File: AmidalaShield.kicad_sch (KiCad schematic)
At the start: 1 part

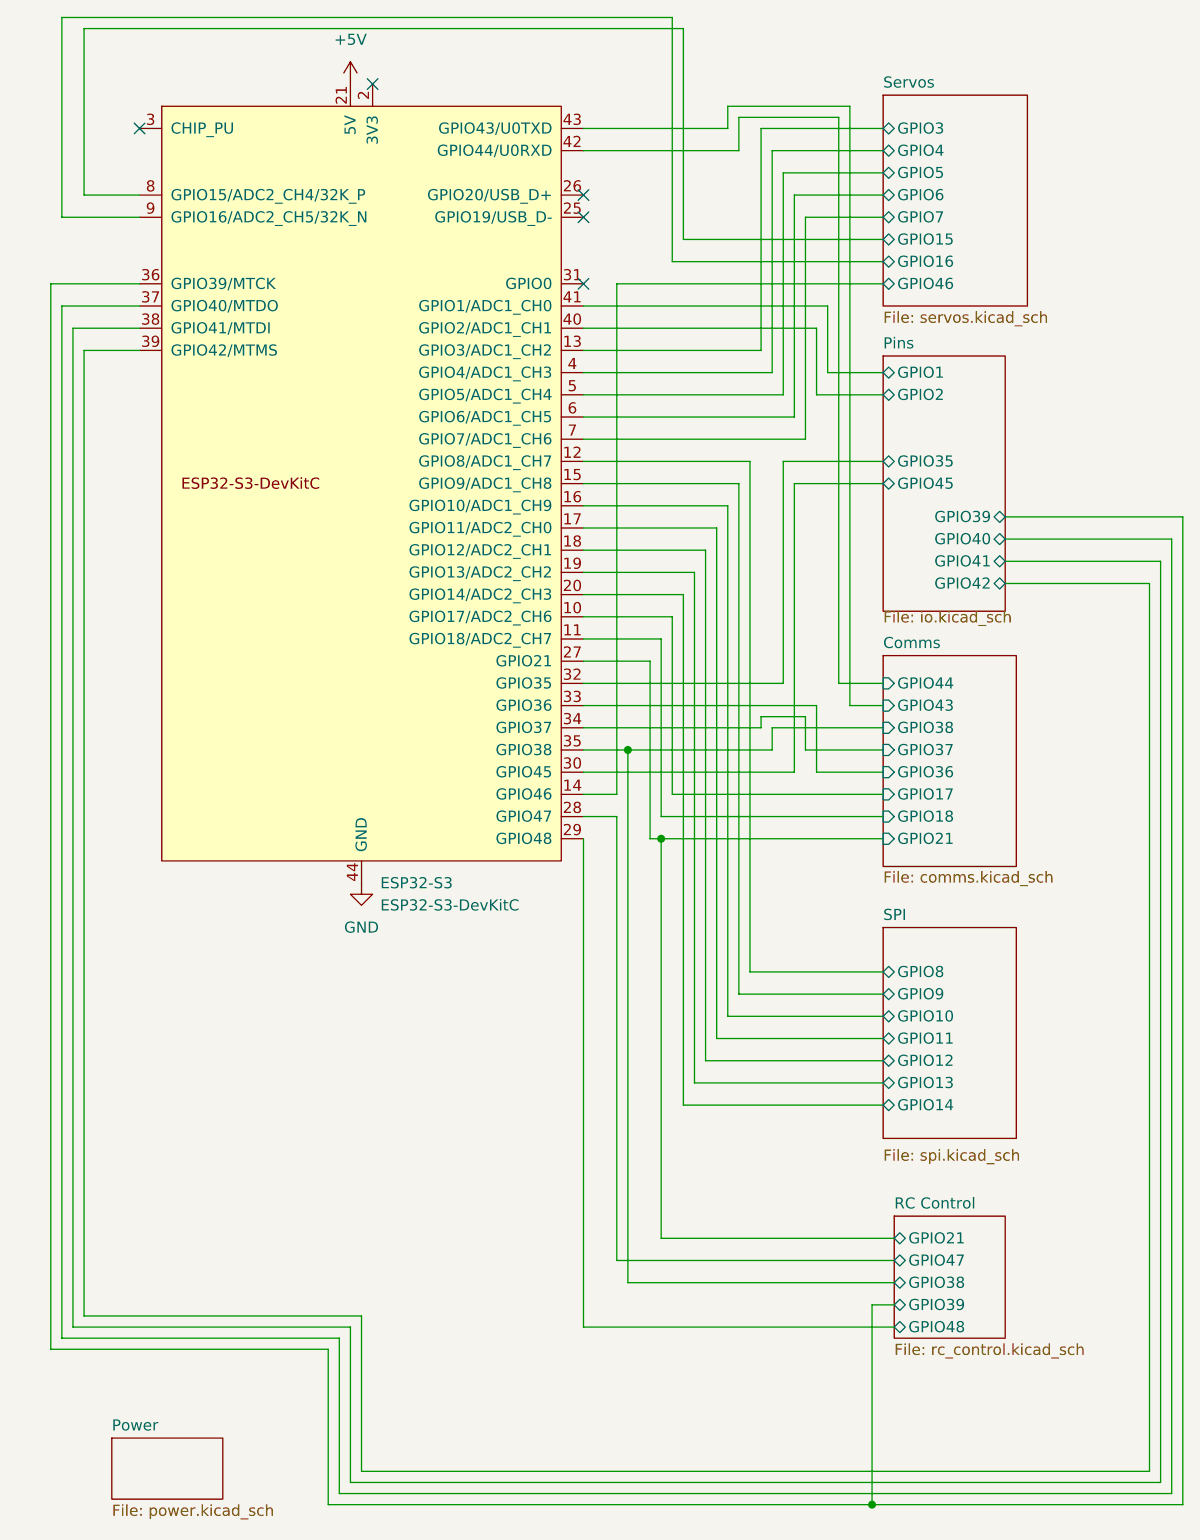
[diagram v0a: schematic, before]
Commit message: Remapped GPIOs for clean routing
This updates the GPIO table so that the traces and vias are far cleaner. Slight repositioning of some pins to account for that. Rebuilt all gerbers and necessary stuff.
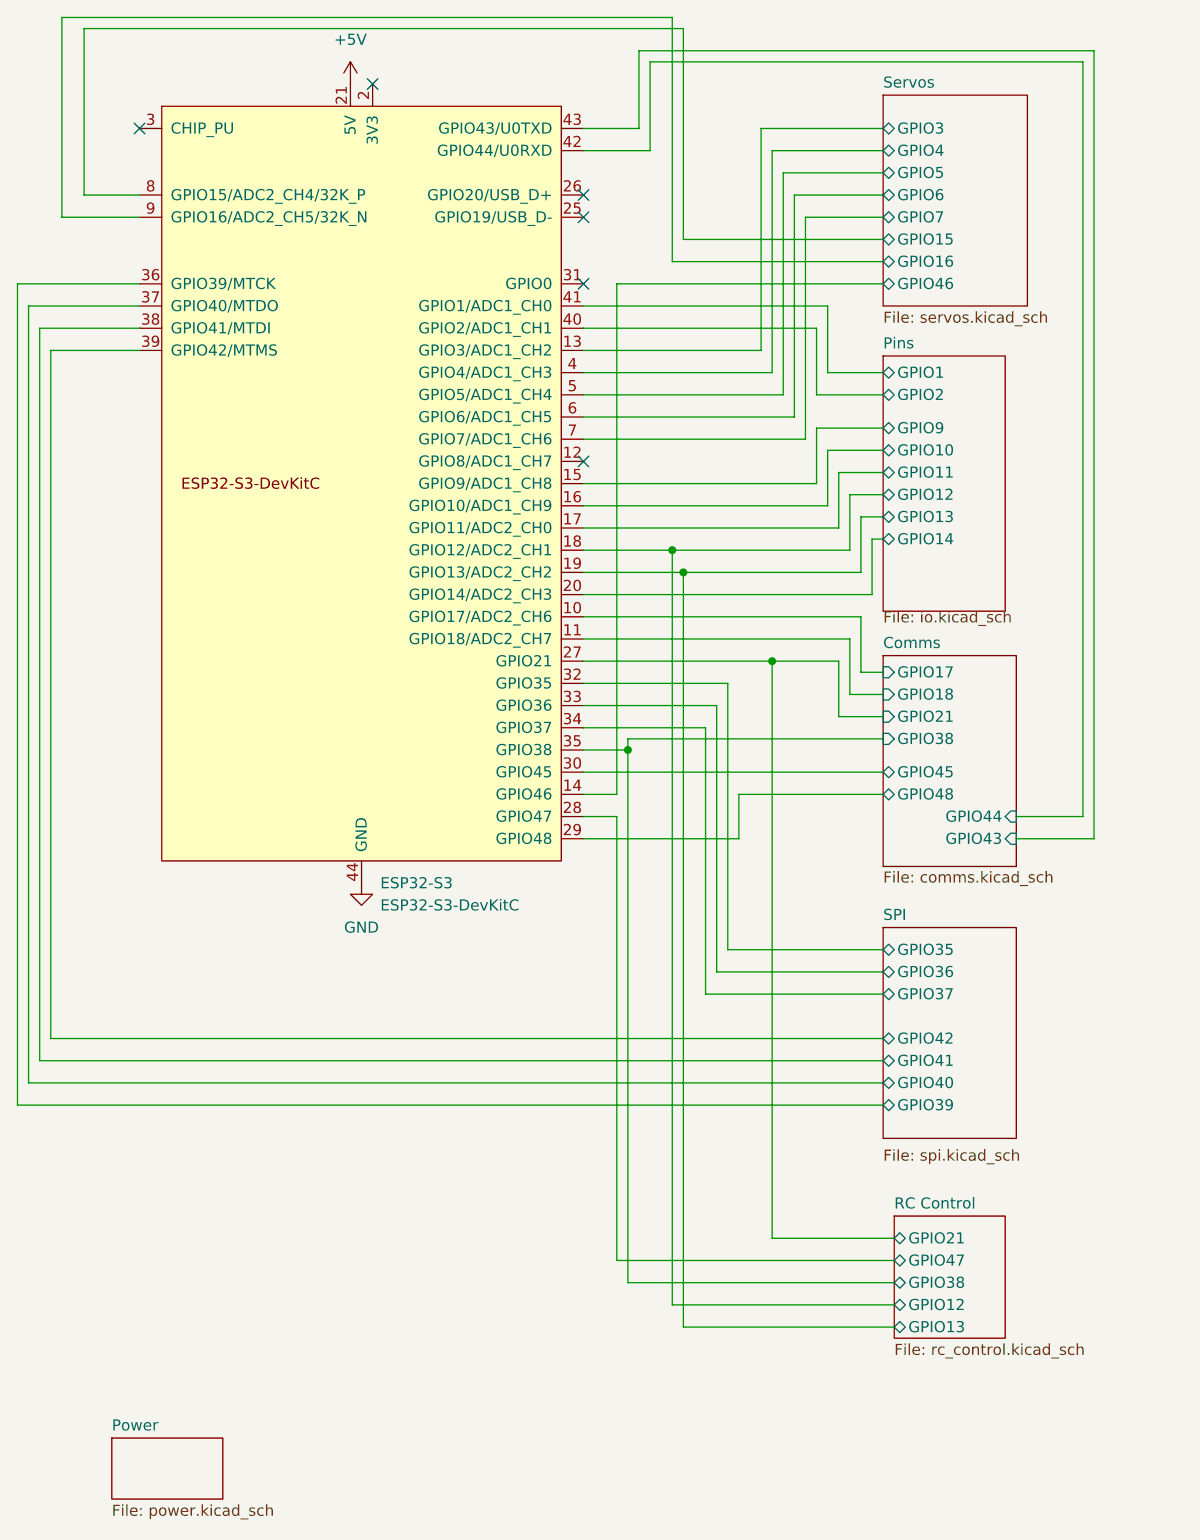
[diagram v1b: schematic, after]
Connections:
- net Comms/GPIO36 renamed SPI/GPIO36
- net Comms/GPIO37 renamed SPI/GPIO37
- net Pins/GPIO35 renamed SPI/GPIO35
- net Pins/GPIO39 renamed SPI/GPIO39
- net Pins/GPIO40 renamed SPI/GPIO40
- net Pins/GPIO41 renamed SPI/GPIO41
- net Pins/GPIO42 renamed SPI/GPIO42
- net Pins/GPIO45 renamed Comms/GPIO45
- net RC Control/GPIO48 renamed Comms/GPIO48
- net SPI/GPIO10 renamed Pins/GPIO10
- net SPI/GPIO11 renamed Pins/GPIO11
- net SPI/GPIO12 renamed Pins/GPIO12
- net SPI/GPIO13 renamed Pins/GPIO13
- net SPI/GPIO14 renamed Pins/GPIO14
- net SPI/GPIO8: no longer names the net of ESP32-S3.12 (GPIO8/ADC1_CH7)
- net SPI/GPIO9 renamed Pins/GPIO9
- no-connect marks 5 -> 6
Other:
- sheet Comms ports: added GPIO45, GPIO48; removed GPIO36, GPIO37
- sheet Pins ports: added GPIO10, GPIO11, GPIO12, GPIO13, GPIO14, GPIO9; removed GPIO35, GPIO39, GPIO40, GPIO41, GPIO42, GPIO45
- sheet RC Control ports: added GPIO12, GPIO13; removed GPIO39, GPIO48
- sheet SPI ports: added GPIO35, GPIO36, GPIO37, GPIO39, GPIO40, GPIO41, GPIO42; removed GPIO10, GPIO11, GPIO12, GPIO13, GPIO14, GPIO8, GPIO9

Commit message: final pass safety check
This verified that the XBee had all the pins wired up correctly with the proper resistor and cap connections. Glad I caught this before getting them fabbed.
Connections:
- net SPI/GPIO8: now reaches ESP32-S3.12 (GPIO8/ADC1_CH7)
- no-connect marks 6 -> 5
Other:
- sheet SPI ports: added GPIO8; removed none
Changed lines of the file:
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@@
-	)
-	(no_connect
-		(at 80.01 66.04)
 	)
 	(no_connect
@@
 	(wire
 		(pts
+			(xy 114.3 129.54) (xy 104.14 129.54)
+		)
+		(stroke
+			(width 0)
+			(type default)
+		)
+	)
+	(wire
+		(pts
 			(xy 109.22 88.9) (xy 101.6 88.9)
 		)
@@
 	(wire
 		(pts
+			(xy 104.14 66.04) (xy 80.01 66.04)
+		)
+		(stroke
+			(width 0)
+			(type default)
+		)
+	)
+	(wire
+		(pts
 			(xy 86.36 19.05) (xy 138.43 19.05)
 		)
@@
 		(pts
 			(xy 114.3 30.48) (xy 101.6 30.48)
+		)
+		(stroke
+			(width 0)
+			(type default)
+		)
+	)
+	(wire
+		(pts
+			(xy 104.14 129.54) (xy 104.14 66.04)
 		)
 		(stroke
@@
 			(effects
 				(font
+					(size 1.27 1.27)
+				)
+				(justify left)
+			)
+		)
+		(pin "GPIO8" bidirectional
+			(at 114.3 129.54 180)
+			(effects
+				(font

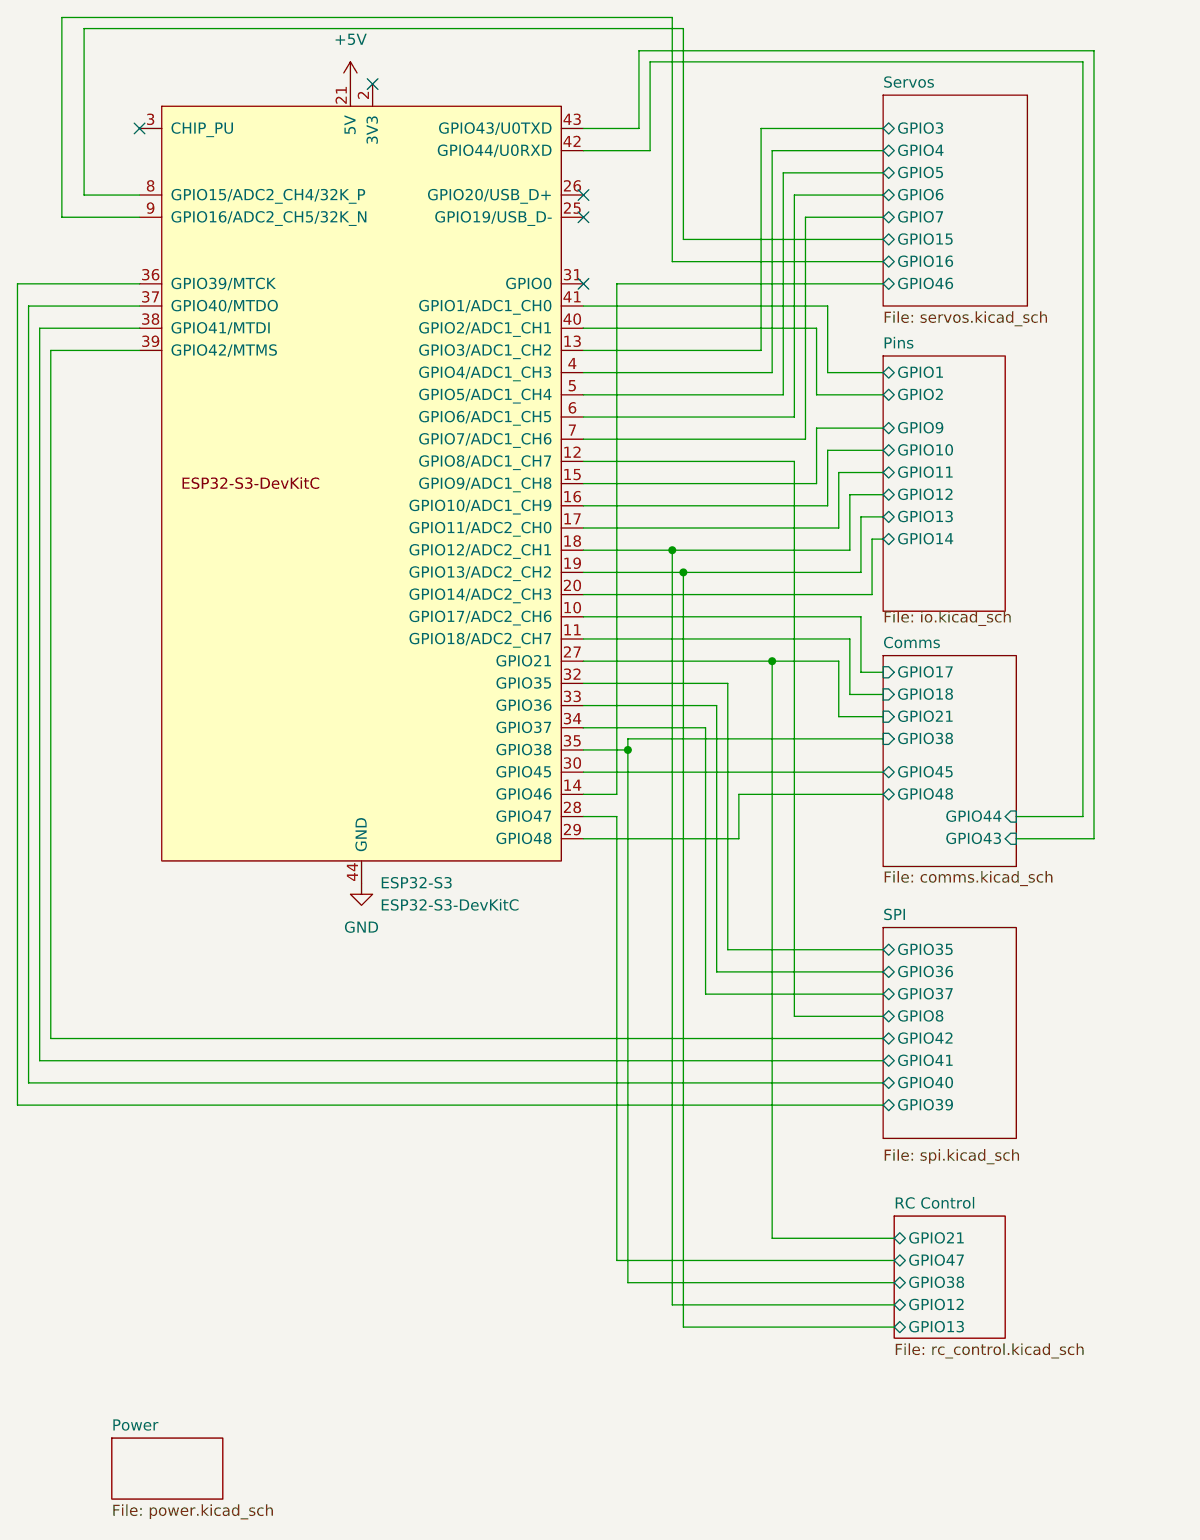
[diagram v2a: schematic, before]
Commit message: Updated to v1.1 to fix issues
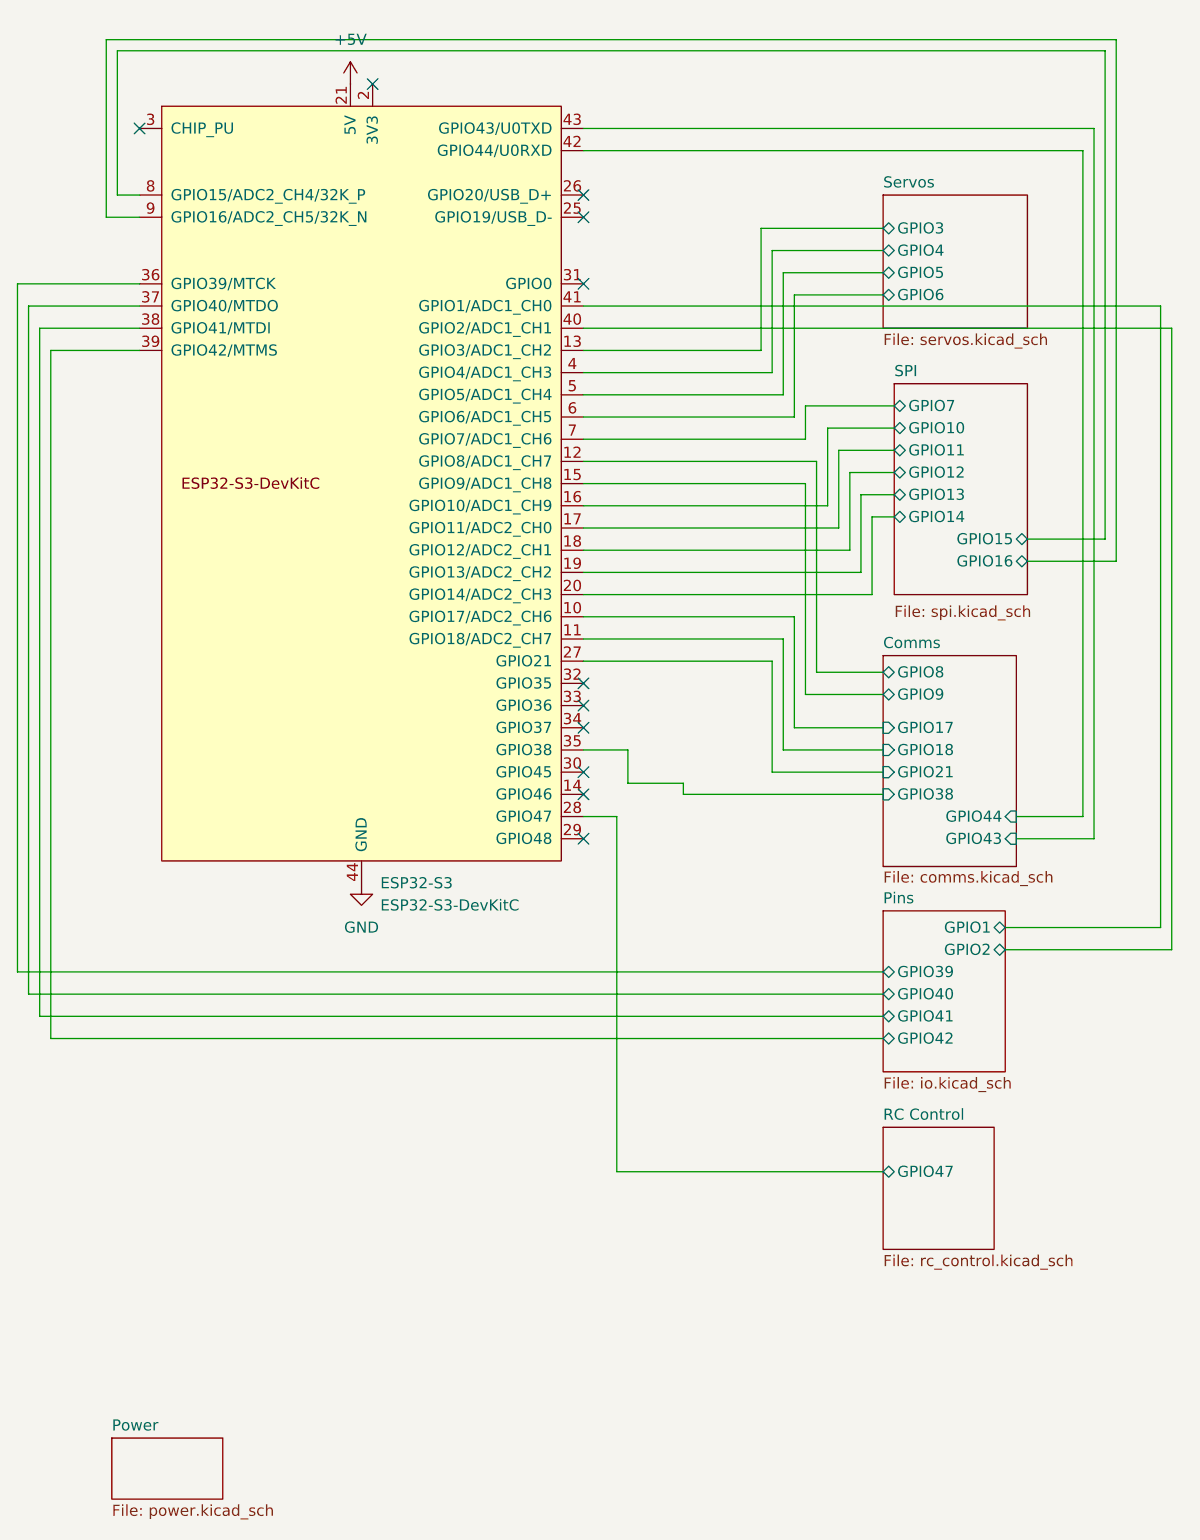
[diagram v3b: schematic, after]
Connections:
- net Comms/GPIO45: no longer names the net of ESP32-S3.30 (GPIO45)
- net Comms/GPIO48: no longer names the net of ESP32-S3.29 (GPIO48)
- net Pins/GPIO10 renamed SPI/GPIO10
- net Pins/GPIO11 renamed SPI/GPIO11
- net Pins/GPIO12 renamed SPI/GPIO12
- net Pins/GPIO13 renamed SPI/GPIO13
- net Pins/GPIO14 renamed SPI/GPIO14
- net Pins/GPIO9 renamed Comms/GPIO9
- net SPI/GPIO35: no longer names the net of ESP32-S3.32 (GPIO35)
- net SPI/GPIO36: no longer names the net of ESP32-S3.33 (GPIO36)
- net SPI/GPIO37: no longer names the net of ESP32-S3.34 (GPIO37)
- net SPI/GPIO39 renamed Pins/GPIO39
- net SPI/GPIO40 renamed Pins/GPIO40
- net SPI/GPIO41 renamed Pins/GPIO41
- net SPI/GPIO42 renamed Pins/GPIO42
- net SPI/GPIO8 renamed Comms/GPIO8
- net Servos/GPIO15 renamed SPI/GPIO15
- net Servos/GPIO16 renamed SPI/GPIO16
- net Servos/GPIO46: no longer names the net of ESP32-S3.14 (GPIO46)
- net Servos/GPIO7 renamed SPI/GPIO7
- no-connect marks 5 -> 11
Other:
- sheet Comms ports: added GPIO8, GPIO9; removed GPIO45, GPIO48
- sheet Pins ports: added GPIO39, GPIO40, GPIO41, GPIO42; removed GPIO10, GPIO11, GPIO12, GPIO13, GPIO14, GPIO9
- sheet RC Control ports: added none; removed GPIO12, GPIO13, GPIO21, GPIO38
- sheet SPI ports: added GPIO10, GPIO11, GPIO12, GPIO13, GPIO14, GPIO15, GPIO16, GPIO7; removed GPIO35, GPIO36, GPIO37, GPIO39, GPIO40, GPIO41, GPIO42, GPIO8
- sheet Servos ports: added none; removed GPIO15, GPIO16, GPIO46, GPIO7
- title: (none) -> Amidala Board

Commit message: Updated to v1.2 to address remaining issues
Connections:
- net +3.3V: now reaches ESP32-S3.1 (3V3), ESP32-S3.2 (3V3)
- no-connect marks 11 -> 10
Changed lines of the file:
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@@
-	)
-	(no_connect
-		(at 55.88 22.86)
 	)
 	(no_connect
@@
 		)
 	)
+	(symbol
+		(lib_id "power:+3.3V")
+		(at 55.88 22.86 0)
+		(unit 1)
+		(exclude_from_sim no)
+		(in_bom yes)
+		(on_board yes)
+		(dnp no)
+		(fields_autoplaced yes)
+		(property "Reference" "#PWR023"
+			(at 55.88 26.67 0)
+			(effects
+				(font
+					(size 1.27 1.27)
+				)
+				(hide yes)
+			)
+		)
+		(property "Value" "+3.3V"
+			(at 55.88 17.78 0)
+			(effects
+				(font
+					(size 1.27 1.27)
+				)
+			)
+		)
+		(property "Footprint" ""
+			(at 55.88 22.86 0)
+			(effects
+				(font
+					(size 1.27 1.27)
+				)
+				(hide yes)
+			)
+		)
+		(property "Datasheet" ""
+			(at 55.88 22.86 0)
+			(effects
+				(font
+					(size 1.27 1.27)
+				)
+				(hide yes)
+			)
+		)
+		(property "Description" "Power symbol creates a global label with name \"+3.3V\""
+			(at 55.88 22.86 0)
+			(effects
+				(font
+					(size 1.27 1.27)
+				)
+				(hide yes)
+			)
+		)
+		(pin "1"
+		)
+		(instances
+			(project "AmidalaShield"
+				(path "/6d8d0000-f03d-4277-95db-0f566c3960c4"
+					(reference "#PWR023")
+					(unit 1)
+				)
+			)
+		)
+	)
